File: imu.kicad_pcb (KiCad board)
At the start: 4 copper layers, 70.8 x 41.2 mm, 39 parts, among them J1 USB_C_Receptacle_USB2.0_16P, J2 JST_PH2.0_01x04, J3 JST_PH2.0_01x04, J4 GPIO0, J5 GPIO1, SW1 SW_Push, SW2 SW_Push, U1 LSM6DSL, U2 LIS2MDL, U3 AMS1117-3.3, U4 ESP32-C3-WROOM-02

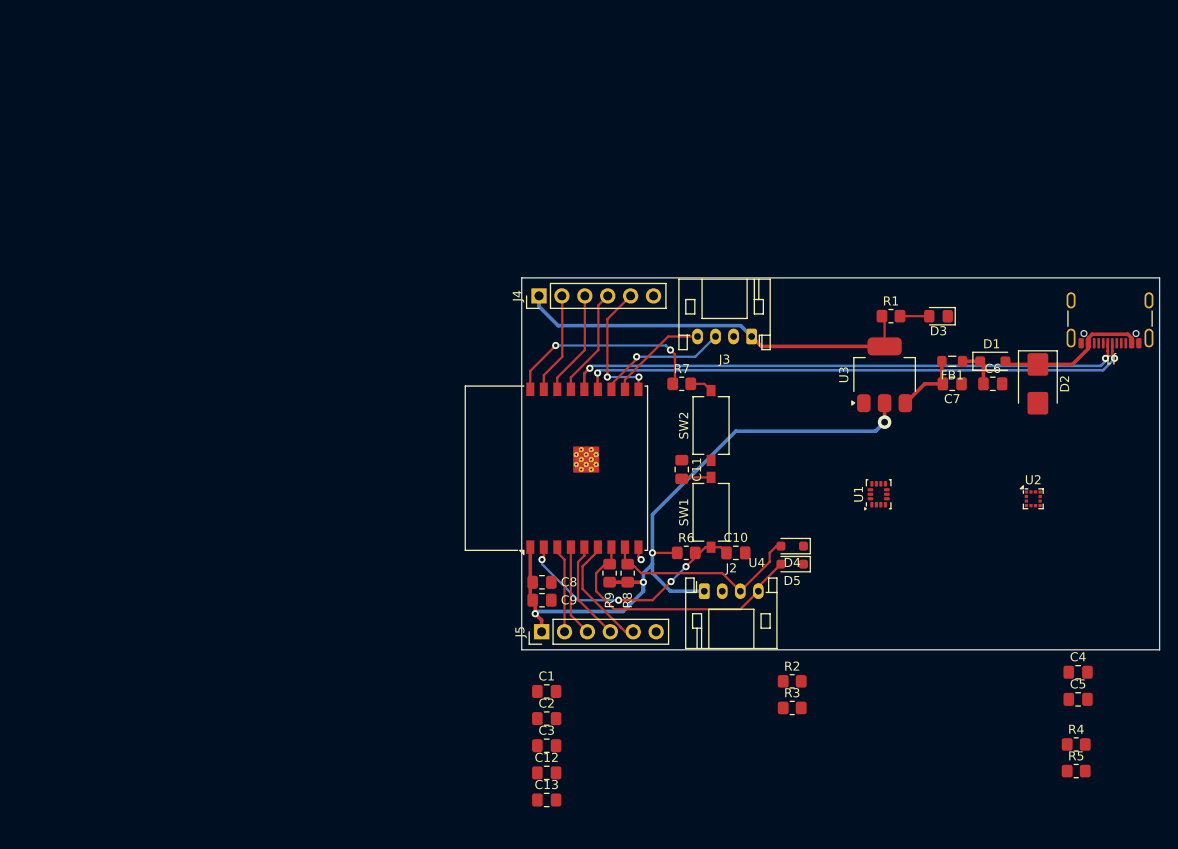
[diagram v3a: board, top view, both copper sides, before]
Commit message: Add Sensors and Silkscreen Adjustments
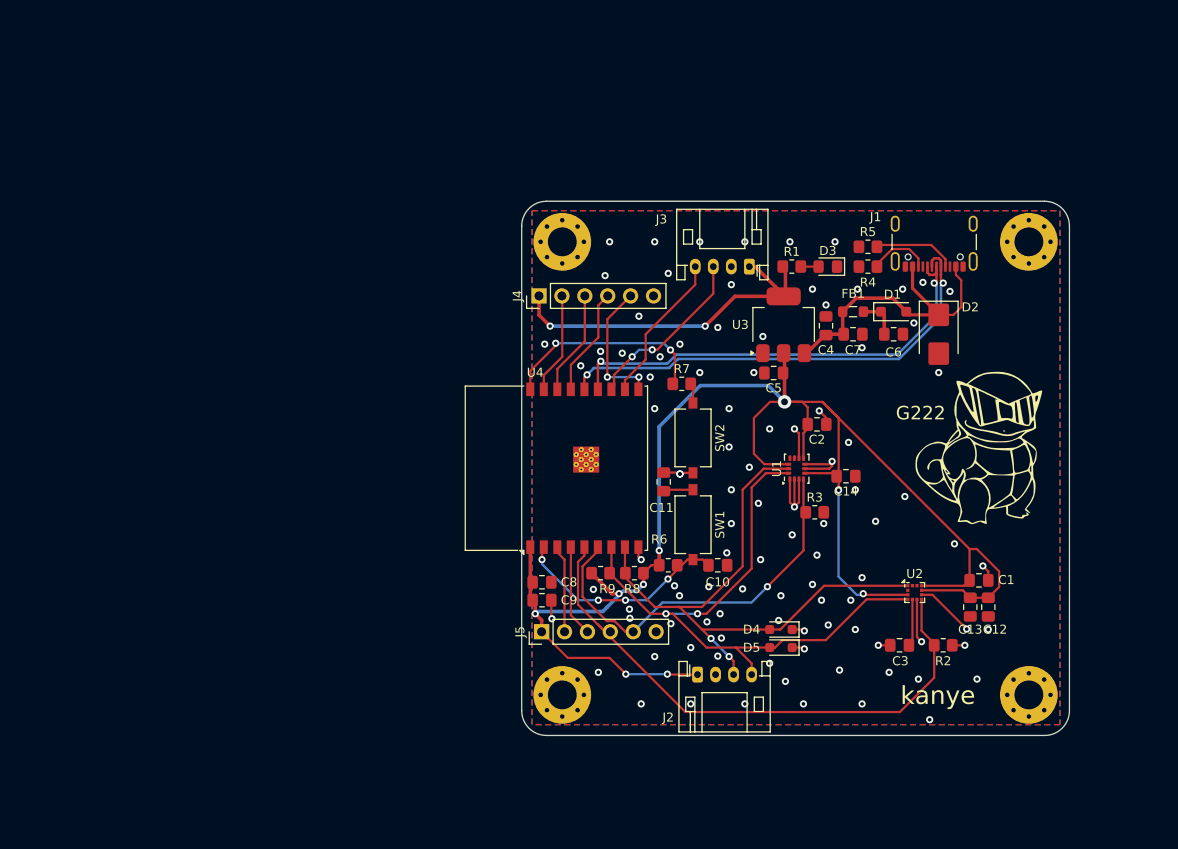
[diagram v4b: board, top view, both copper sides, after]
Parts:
- added C14: 100nF, Capacitor_SMD:C_0805_2012Metric_Pad1.18x1.45mm_HandSolder, F.Cu at (151.2, 69.2)
- added G222: LOGO, Graphics:Sunglasses_Squirtle, F.Cu at (166.5, 66.0)
- added REF**: MountingHole_3.2mm_M3_Pad_Via, MountingHole:MountingHole_3.2mm_M3_Pad_Via, F.Cu at (119.8, 43.2)
- added REF**: MountingHole_3.2mm_M3_Pad_Via, MountingHole:MountingHole_3.2mm_M3_Pad_Via, F.Cu at (119.8, 93.5)
- added REF**: MountingHole_3.2mm_M3_Pad_Via, MountingHole:MountingHole_3.2mm_M3_Pad_Via, F.Cu at (171.5, 43.2)
- added REF**: MountingHole_3.2mm_M3_Pad_Via, MountingHole:MountingHole_3.2mm_M3_Pad_Via, F.Cu at (171.5, 93.5)
- moved R5 62.6 mm to (153.7, 43.8)
- moved R4 57.8 mm to (153.7, 46.0)
- moved C12 52.3 mm to (167.0, 83.8), turned to 90 degrees
- moved C13 51.6 mm to (165.0, 83.8), turned to 90 degrees
- moved C5 49.5 mm to (143.2, 57.8), turned to 180 degrees
- moved C1 49.5 mm to (166.0, 80.8)
- moved C4 47.5 mm to (149.0, 52.6), turned to 90 degrees
- moved C2 44.3 mm to (148.0, 63.5), turned to 180 degrees
- moved C3 40.7 mm to (157.2, 88.0)
- moved R3 21.8 mm to (147.8, 73.2)
- moved J1 21.3 mm to (161.0, 42.3)
- moved R2 17.2 mm to (162.0, 88.0)
- moved U2 16.8 mm to (158.8, 82.2)
- moved D3 13.5 mm to (149.2, 46.0)
- moved U3 12.5 mm to (144.3, 52.5)
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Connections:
- J5 pad 4: IO6 -> INT_MAG
- J5 pad 5: IO7 -> INT_IMU
- U4 pad 5: IO6 -> INT_MAG
- U4 pad 6: IO7 -> INT_IMU
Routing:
- net +3V3: track 124.0 -> 233.1 mm, vias 4 -> 11
- net INT_MAG: track 0.00 -> 63.7 mm
- net SCL: track 22.9 -> 69.2 mm, vias 0 -> 2
- net GND: track 1.51 -> 47.7 mm, vias 1 -> 99
- net INT_IMU: track 0.00 -> 44.0 mm, vias 0 -> 1
- net SDA: track 29.7 -> 70.7 mm, vias 0 -> 2
- net IO7: track 12.9 -> 0.00 mm
- net IO6: track 11.2 -> 0.00 mm
- net +5V: track 24.6 -> 35.2 mm
- net USB_D-: track 62.5 -> 52.0 mm
- net USB_D+: track 61.7 -> 51.5 mm
- net Net-(J1-CC1): track 0.00 -> 9.16 mm
- net Net-(J1-CC2): track 0.00 -> 6.91 mm
- net RX0: track 11.1 -> 16.8 mm
- net Net-(U2-C1): track 0.00 -> 5.15 mm
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- added copper zone on B.Cu, net GND
- added copper zone on F.Cu, net GND
- added copper zone on In1.Cu, net GND
- added copper zone on In2.Cu, net GND
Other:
- board size 70.8 x 41.2 mm -> 60.8 x 59.2 mm
- board text added: "Vision IO Board V1.1"
- board text added: "kanye"
